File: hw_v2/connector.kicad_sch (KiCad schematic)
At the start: 22 parts, among them J1 Conn_02x24_Counter_Clockwise, J14 Conn_01x04, U11 L78M05ABDT-TR, U19 L78M05ABDT-TR, U25 74LVC2G17, U26 74LVC2G17, U8 AMS1117-3.3

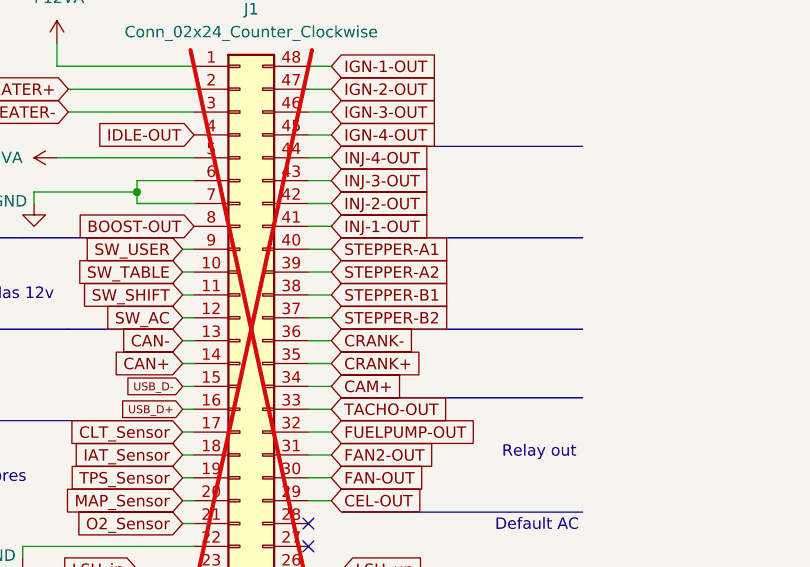
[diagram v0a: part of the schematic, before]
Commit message: wip routing iny/ign drivers
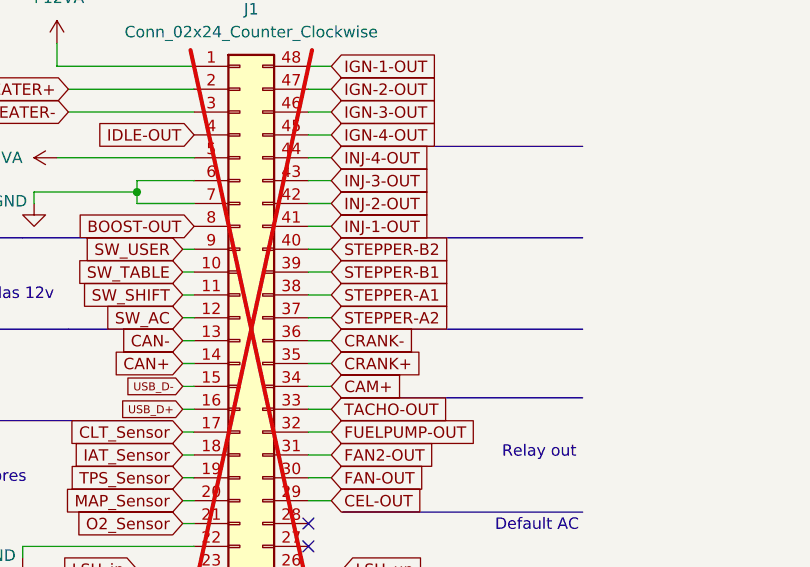
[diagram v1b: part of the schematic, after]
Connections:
- net STEPPER-A1: now also J1.38 (Pin_38); no longer J1.40 (Pin_40)
- net STEPPER-A2: now also J1.37 (Pin_37); no longer J1.39 (Pin_39)
- net STEPPER-B1: now also J1.39 (Pin_39); no longer J1.38 (Pin_38)
- net STEPPER-B2: now also J1.40 (Pin_40); no longer J1.37 (Pin_37)

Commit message: wip mcu routing
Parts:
- removed JP10, JP9: SolderJumper_3_Bridged12, Jumper:SolderJumper-3_P1.3mm_Bridged2Bar12_Pad1.0x1.5mm, symbol Jumper:SolderJumper_3_Bridged12
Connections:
- net LSU_ip: now also J1.28 (Pin_28); no longer J1.23 (Pin_23)
- net LSU_rtrim: now also J1.24 (Pin_24); no longer J1.25 (Pin_25)
- net LSU_un: now also J1.23 (Pin_23); no longer J1.26 (Pin_26)
- net LSU_vm: now also J1.27 (Pin_27); no longer J1.24 (Pin_24)
- net USART_2_RX: now also J14.3 (Pin_3)
- net USART_2_TX: now also J14.4 (Pin_4)
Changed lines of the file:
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@@
 	)
 	(no_connect
-		(at 86.36 106.68)
+		(at 86.36 111.76)
 	)
 	(no_connect
-		(at 86.36 104.14)
+		(at 86.36 109.22)
 	)
 	(wire
@@
 	(wire
 		(pts
-			(xy 73.66 138.43) (xy 101.6 138.43)
+			(xy 73.66 138.43) (xy 78.74 138.43)
 		)
 		(stroke
@@
 	(wire
 		(pts
-			(xy 101.6 137.16) (xy 101.6 138.43)
-		)
-		(stroke
-			(width 0)
-			(type default)
-		)
-	)
-	(wire
-		(pts
 			(xy 264.16 74.93) (xy 251.46 74.93)
 		)
@@
 	(wire
 		(pts
-			(xy 90.17 109.22) (xy 86.36 109.22)
+			(xy 90.17 104.14) (xy 86.36 104.14)
 		)
 		(stroke
@@
 	(wire
 		(pts
-			(xy 73.66 140.97) (xy 101.6 140.97)
+			(xy 73.66 140.97) (xy 78.74 140.97)
 		)
 		(stroke
@@
 	(wire
 		(pts
-			(xy 90.17 111.76) (xy 86.36 111.76)
+			(xy 90.17 106.68) (xy 86.36 106.68)
 		)
 		(stroke
@@
 	(global_label "USART_2_TX"
 		(shape input)
-		(at 96.52 133.35 180)
+		(at 78.74 138.43 0)
 		(fields_autoplaced yes)
 		(effects
@@
 				(size 0.8 0.8)
 			)
-			(justify right)
+			(justify left)
 		)
 		(property "Intersheetrefs" "${INTERSHEET_REFS}"
-			(at 87.5922 133.35 0)
+			(at 87.6678 138.43 0)
 			(effects
 				(font
 					(size 1.27 1.27)
 				)
-				(justify right)
+				(justify left)
 				(hide yes)
 			)
@@
 	(global_label "LSU_rtrim"
 		(shape input)
-		(at 90.17 111.76 0)
+		(at 67.31 111.76 180)
 		(fields_autoplaced yes)
 		(effects
@@
 				(size 1.27 1.27)
 			)
-			(justify left)
+			(justify right)
 		)
 		(property "Intersheetrefs" "${INTERSHEET_REFS}"
-			(at 102.2871 111.76 0)
+			(at 57.4911 111.76 0)
 			(effects
 				(font
 					(size 1.27 1.27)
 				)
-				(justify left)
+				(justify right)
 				(hide yes)
 			)
@@
 		)
 	)
-	(global_label "USART_2_RX"
-		(shape input)
-		(at 106.68 133.35 0)
-		(fields_autoplaced yes)
-		(effects
-			(font
-				(size 0.8 0.8)
-			)
-			(justify left)
-		)
-		(property "Intersheetrefs" "${INTERSHEET_REFS}"
-			(at 115.7983 133.35 0)
-			(effects
-				(font
-					(size 1.27 1.27)
-				)
-				(justify left)
-				(hide yes)
-			)
-		)
-	)
 	(global_label "IGN-1-OUT"
 		(shape input)
@@
 	(global_label "LSU_un"
 		(shape input)
-		(at 90.17 109.22 0)
+		(at 67.31 109.22 180)
 		(fields_autoplaced yes)
 		(effects
@@
 				(size 1.27 1.27)
 			)
-			(justify left)
+			(justify right)
 		)
 		(property "Intersheetrefs" "${INTERSHEET_REFS}"
-			(at 99.9889 109.22 0)
+			(at 55.1929 109.22 0)
 			(effects
 				(font
 					(size 1.27 1.27)
 				)
-				(justify left)
+				(justify right)
 				(hide yes)
 			)
@@
 		)
 	)
-	(global_label "USART_2_TX"
-		(shape input)
-		(at 96.52 144.78 180)
-		(fields_autoplaced yes)
-		(effects
-			(font
-				(size 0.8 0.8)
-			)
-			(justify right)
-		)
-		(property "Intersheetrefs" "${INTERSHEET_REFS}"
-			(at 87.5922 144.78 0)
-			(effects
-				(font
-					(size 1.27 1.27)
-				)
-				(justify right)
-				(hide yes)
-			)
-		)
-	)
 	(global_label "TPS_Sensor"
 		(shape input)
@@
 	(global_label "USART_2_RX"
 		(shape input)
-		(at 106.68 144.78 0)
+		(at 78.74 140.97 0)
 		(fields_autoplaced yes)
 		(effects
@@
 		)
 		(property "Intersheetrefs" "${INTERSHEET_REFS}"
-			(at 115.7983 144.78 0)
+			(at 87.8583 140.97 0)
 			(effects
 				(font
@@
 	(global_label "LSU_vm"
 		(shape input)
-		(at 67.31 111.76 180)
+		(at 90.17 106.68 0)
 		(fields_autoplaced yes)
 		(effects
@@
 				(size 1.27 1.27)
 			)
-			(justify right)
+			(justify left)
 		)
 		(property "Intersheetrefs" "${INTERSHEET_REFS}"
-			(at 57.1282 111.76 0)
+			(at 99.4447 106.68 0)
 			(effects
 				(font
 					(size 1.27 1.27)
 				)
-				(justify right)
+				(justify left)
 				(hide yes)
 			)
@@
 	(global_label "LSU_ip"
 		(shape input)
-		(at 67.31 109.22 180)
+		(at 90.17 104.14 0)
 		(fields_autoplaced yes)
 		(effects
@@
 				(size 1.27 1.27)
 			)
-			(justify right)
+			(justify left)
 		)
 		(property "Intersheetrefs" "${INTERSHEET_REFS}"
-			(at 58.0353 109.22 0)
+			(at 100.3518 104.14 0)
 			(effects
 				(font
 					(size 1.27 1.27)
 				)
-				(justify right)
+				(justify left)
 				(hide yes)
 			)
@@
 	)
 	(symbol
-		(lib_id "Jumper:SolderJumper_3_Bridged12")
-		(at 101.6 133.35 0)
-		(unit 1)
-		(exclude_from_sim no)
-		(in_bom no)
-		(on_board yes)
-		(dnp yes)
-		(property "Reference" "JP9"
-			(at 101.6 129.54 0)
-			(effects
-				(font
-					(size 1.27 1.27)
-				)
-				(hide yes)
-			)
-		)
-		(property "Value" "SolderJumper_3_Bridged12"
-			(at 101.6 127 0)
-			(effects
-				(font
-					(size 1.27 1.27)
-				)
-				(hide yes)
-			)
-		)
-		(property "Footprint" "Jumper:SolderJumper-3_P1.3mm_Bridged2Bar12_Pad1.0x1.5mm"
-			(at 101.6 133.35 0)
-			(effects
-				(font
-					(size 1.27 1.27)
-				)
-				(hide yes)
-			)
-		)
-		(property "Datasheet" "~"
-			(at 101.6 133.35 0)
-			(effects
-				(font
-					(size 1.27 1.27)
-				)
-				(hide yes)
-			)
-		)
-		(property "Description" "3-pole Solder Jumper, pins 1+2 closed/bridged"
-			(at 101.6 133.35 0)
-			(effects
-				(font
-					(size 1.27 1.27)
-				)
-				(hide yes)
-			)
-		)
-		(pin "3"
-		)
-		(pin "2"
-		)
-		(pin "1"
-		)
-		(instances
-			(project "hw_v1"
-				(path "/b3feb07e-be80-40e1-bd13-6cd54c2f8b0c/312f3a58-86c6-4c57-9da0-ed62046efef3"
-					(reference "JP9")
-					(unit 1)
-				)
-			)
-		)
-	)
-	(symbol
 		(lib_id "Regulator_Linear:AMS1117-3.3")
 		(at 184.15 30.48 0)
@@
 					(unit 1)
 				)
-			)
-		)
-	)
-	(symbol
-		(lib_name "SolderJumper_3_Bridged12_1")
-		(lib_id "Jumper:SolderJumper_3_Bridged12")
-		(at 101.6 144.78 180)
-		(unit 1)
-		(exclude_from_sim no)
-		(in_bom no)
-		(on_board yes)
-		(dnp yes)
-		(fields_autoplaced yes)
-		(property "Reference" "JP10"
-			(at 101.6 148.59 0)
-			(effects
-				(font
-					(size 1.27 1.27)
-				)
-				(hide yes)
-			)
-		)
-		(property "Value" "SolderJumper_3_Bridged12"
-			(at 101.6 151.13 0)
-			(effects
-				(font
-					(size 1.27 1.27)
-				)
-				(hide yes)
-			)
-		)
-		(property "Footprint" "Jumper:SolderJumper-3_P1.3mm_Bridged2Bar12_Pad1.0x1.5mm"
-			(at 101.6 144.78 0)
-			(effects
-				(font
-					(size 1.27 1.27)
-				)
-				(hide yes)
-			)
-		)
-		(property "Datasheet" "~"
-			(at 101.6 144.78 0)
-			(effects
-				(font
-					(size 1.27 1.27)
-				)
-				(hide yes)
-			)
-		)
-		(property "Description" "3-pole Solder Jumper, pins 1+2 closed/bridged"
-			(at 101.6 144.78 0)
-			(effects
-				(font
-					(size 1.27 1.27)
-				)
-				(hide yes)
-			)
-		)
-		(pin "3"
-		)
-		(pin "2"
-		)
-		(pin "1"
-		)
-		(instances
-			(project "hw_v1"
-				(path "/b3feb07e-be80-40e1-bd13-6cd54c2f8b0c/312f3a58-86c6-4c57-9da0-ed62046efef3"
-					(reference "JP10")
-					(unit 1)
-				)

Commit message: update ADC oamp
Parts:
- U25, U26: LCSC (none) -> C80500
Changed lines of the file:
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@@
 			)
 		)
+		(property "LCSC" "C80500"
+			(at 239.522 143.51 0)
+			(effects
+				(font
+					(size 1.27 1.27)
+				)
+				(hide yes)
+			)
+		)
 		(pin "4"
 		)
@@
 			)
 		)
+		(property "LCSC" "C80500"
+			(at 269.24 146.0499 0)
+			(effects
+				(font
+					(size 1.27 1.27)
+				)
+				(hide yes)
+			)
+		)
 		(pin "3"
 		)
@@
 			)
 		)
+		(property "LCSC" "C80500"
+			(at 254 77.724 0)
+			(effects
+				(font
+					(size 1.27 1.27)
+				)
+				(hide yes)
+			)
+		)
 		(pin "3"
 		)
@@
 			)
 		)
+		(property "LCSC" "C80500"
+			(at 237.49 63.5 0)
+			(effects
+				(font
+					(size 1.27 1.27)
+				)
+				(hide yes)
+			)
+		)
 		(pin "3"
 		)
@@
 			)
 		)
+		(property "LCSC" "C80500"
+			(at 240.538 86.106 0)
+			(effects
+				(font
+					(size 1.27 1.27)
+				)
+				(hide yes)
+			)
+		)
 		(pin "4"
 		)
@@
 			(effects
 				(font
+					(size 1.27 1.27)
+				)
+				(hide yes)
+			)
+		)
+		(property "LCSC" "C80500"
+			(at 257.302 94.996 0)
+			(effects
+				(font
